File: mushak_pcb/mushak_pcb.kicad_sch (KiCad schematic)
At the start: 46 parts, among them J1 Conn_01x04_Male, J10 IR_1, J11 AS5600_1, J12 IR_2, J13 AS5600_2, J14 IR_3, J15 ToF, J16 IR_4, J2 Conn_01x02_Female, J3 BLE_Conn, Q1 DMN3065LW-7, SW1 SW_Push, SW2 SW_Push, U2 TLV1117LV30DCYT, U6 STM32F405RGTx, Y1 25Mhz, Y2 32.769kHz

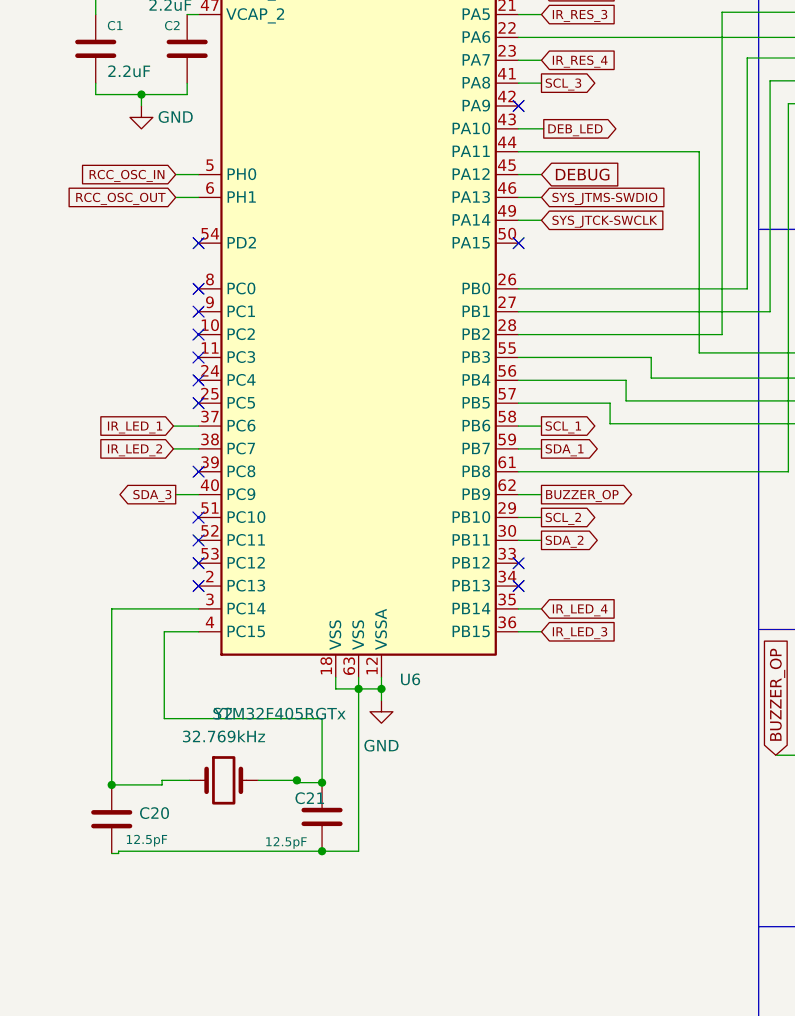
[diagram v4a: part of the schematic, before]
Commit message: corrected encoder and motor driver schematics
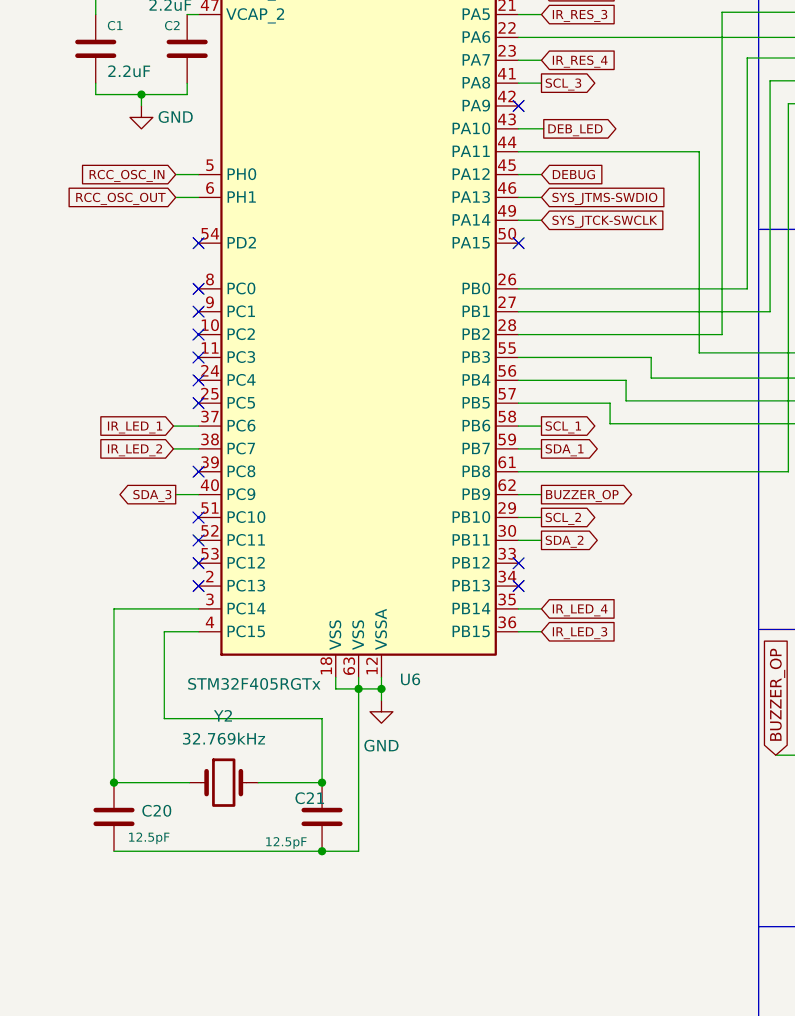
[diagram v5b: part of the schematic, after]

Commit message: VL6180x part routed
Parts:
- C17: footprint Capacitor_SMD:C_0402_1005Metric -> Capacitor_SMD:C_0201_0603Metric
- J1: footprint Connector_JST:JST_SH_SM04B-SRSS-TB_1x04-1MP_P1.00mm_Horizontal -> Connector_JST:JST_SH_BM04B-SRSS-TB_1x04-1MP_P1.00mm_Vertical
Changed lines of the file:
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@@
       (effects (font (size 1.27 1.27)) (justify left))
     )
-    (property "Footprint" "Capacitor_SMD:C_0402_1005Metric" (id 2) (at 261.3152 97.79 0)
+    (property "Footprint" "Capacitor_SMD:C_0201_0603Metric" (id 2) (at 261.3152 97.79 0)
       (effects (font (size 1.27 1.27)) hide)
     )
@@
     (property "Reference" "J1" (id 0) (at 225.425 140.97 0))
     (property "Value" "Conn_01x04_Male" (id 1) (at 225.425 143.51 0))
-    (property "Footprint" "Connector_JST:JST_SH_SM04B-SRSS-TB_1x04-1MP_P1.00mm_Horizontal" (id 2) (at 224.79 148.59 0)
+    (property "Footprint" "Connector_JST:JST_SH_BM04B-SRSS-TB_1x04-1MP_P1.00mm_Vertical" (id 2) (at 224.79 148.59 0)
       (effects (font (size 1.27 1.27)) hide)
     )
@@
     )
     (path "/298d7f54-382e-4035-82e6-d12685de15e8"
-      (reference "C17") (unit 1) (value "0.01uF") (footprint "Capacitor_SMD:C_0402_1005Metric")
+      (reference "C17") (unit 1) (value "0.01uF") (footprint "Capacitor_SMD:C_0201_0603Metric")
     )
     (path "/abd9de0a-decf-4e5d-8587-e1d96a7dcb2e"
@@
     )
     (path "/cb44acba-527a-4750-b41f-72d265c3f4c8/585e9309-f78f-4786-920e-5e445300fb5d"
-      (reference "C31") (unit 1) (value "0.01uf") (footprint "Capacitor_SMD:C_0402_1005Metric")
+      (reference "C31") (unit 1) (value "0.01uf") (footprint "Capacitor_SMD:C_0201_0603Metric")
     )
     (path "/cb44acba-527a-4750-b41f-72d265c3f4c8/b5b8bfc3-6876-47ed-8af9-97827171e9fe"
@@
     )
     (path "/533065b9-0d82-495b-9749-a6ba34793884"
-      (reference "J1") (unit 1) (value "Conn_01x04_Male") (footprint "Connector_JST:JST_SH_SM04B-SRSS-TB_1x04-1MP_P1.00mm_Horizontal")
+      (reference "J1") (unit 1) (value "Conn_01x04_Male") (footprint "Connector_JST:JST_SH_BM04B-SRSS-TB_1x04-1MP_P1.00mm_Vertical")
     )
     (path "/694b3d6e-79ba-4555-820c-469fe372e4c1"
@@
       (reference "R26") (unit 1) (value "47k") (footprint "Resistor_SMD:R_0201_0603Metric")
     )
-    (path "/2c73dddc-4bab-40a4-8c83-c5c599e93cb7/7a42c4f7-316d-483d-a774-55d4e08aacd6"
-      (reference "R27") (unit 1) (value "4.7k") (footprint "")
-    )
     (path "/b266ad3c-1d50-4b2b-8a1e-c69f93195963"

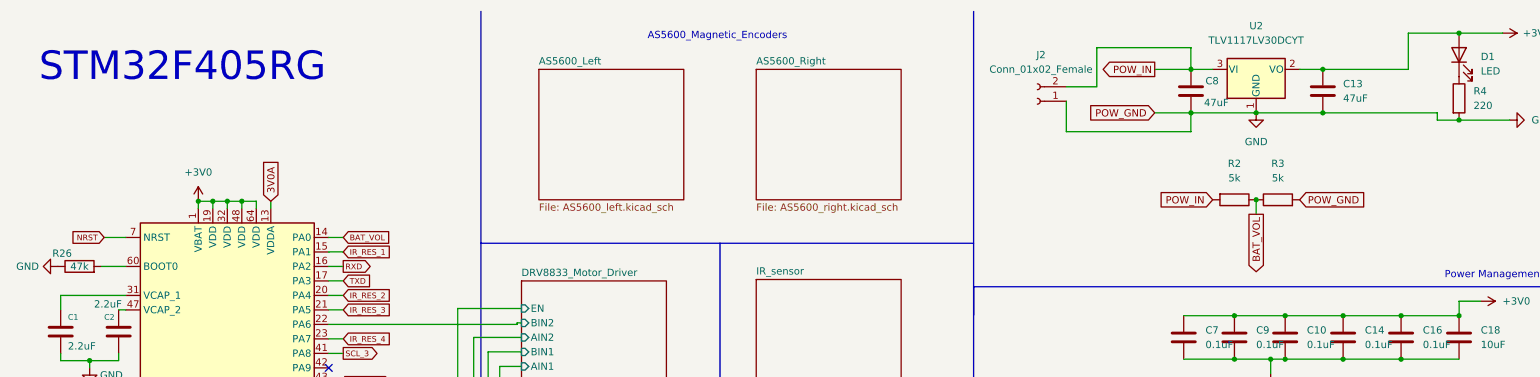
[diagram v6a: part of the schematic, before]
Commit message: changed footprint of passive components
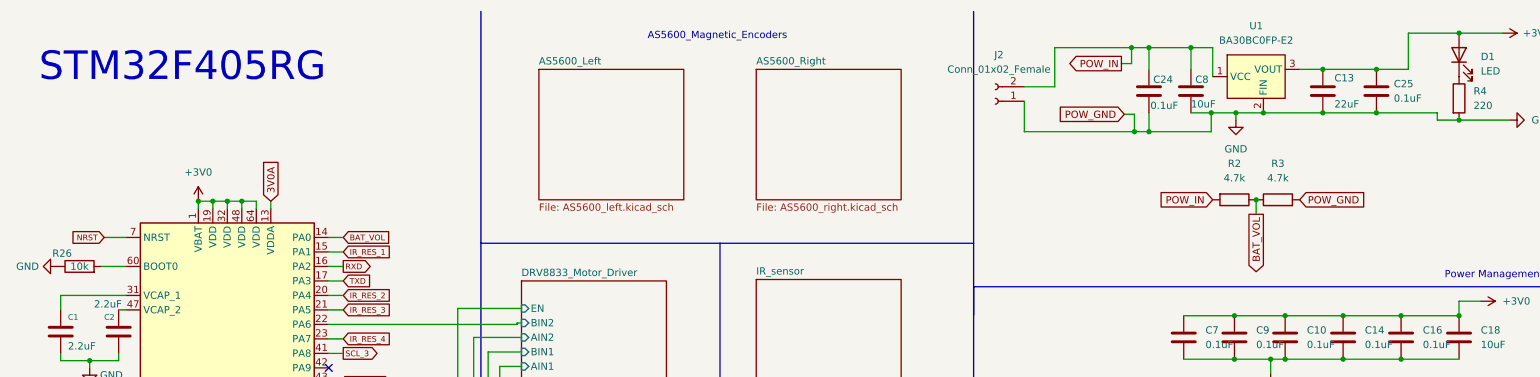
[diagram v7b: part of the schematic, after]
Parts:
- removed U2: TLV1117LV30DCYT, SOT230P700X180-4N:SOT230P700X180-4N, symbol Regulator_Linear:AMS1117-3.3
- added C24, C25: 0.1uF, Capacitor_SMD:C_0402_1005Metric, symbol Device:C
- added U1: BA30BC0FP-E2, IPD50P04P4L-11:DPAK228P998X235-3N, symbol BA30BC0FP-E2:BA30BC0FP-E2
- C1, C12, C18, C19, C2: footprint Capacitor_SMD:C_0402_1005Metric -> Capacitor_SMD:C_0603_1608Metric
- C10, C16, C17, C3, C4, C7, C9: footprint Capacitor_SMD:C_0201_0603Metric -> Capacitor_SMD:C_0402_1005Metric
- C13: value 47uF -> 22uF; footprint Capacitor_SMD:C_0805_2012Metric -> Capacitor_SMD:C_0603_1608Metric
- C8: value 47uF -> 10uF; footprint Capacitor_SMD:C_0805_2012Metric -> Capacitor_SMD:C_0603_1608Metric
- J2: footprint Connector_JST:JST_EH_B2B-EH-A_1x02_P2.50mm_Vertical -> Connector_JST:JST_SHL_SM02B-SHLS-TF_1x02-1MP_P1.00mm_Horizontal
- J3: footprint Connector_PinHeader_2.54mm:PinHeader_1x04_P2.54mm_Vertical -> Connector_JST:JST_SH_BM04B-SRSS-TB_1x04-1MP_P1.00mm_Vertical
- R2, R3: value 5k -> 4.7k; footprint Resistor_SMD:R_0201_0603Metric -> Resistor_SMD:R_0402_1005Metric
- R21: footprint Resistor_SMD:R_0402_1005Metric -> Resistor_SMD:R_0603_1608Metric
- R26: value 47k -> 10k; footprint Resistor_SMD:R_0201_0603Metric -> Resistor_SMD:R_0402_1005Metric
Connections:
- net +3V0: now also C25.1, U1.3 (VOUT)
- net GND: now also C24.2, C25.2, U1.2 (FIN)
- net POW_IN: now also C24.1, U1.1 (VCC)
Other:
- moved on the sheet: J2
